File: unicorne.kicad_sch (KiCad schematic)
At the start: 17 parts, among them J1 Battery, J2 TPS43, J3 Expansion, J4 GPIO, J5 PAW3395 / PMW3360, Q1 AO3401A, Q2 2N7002, SW43 Power, SW44 Reset, U1 nice!nano v2

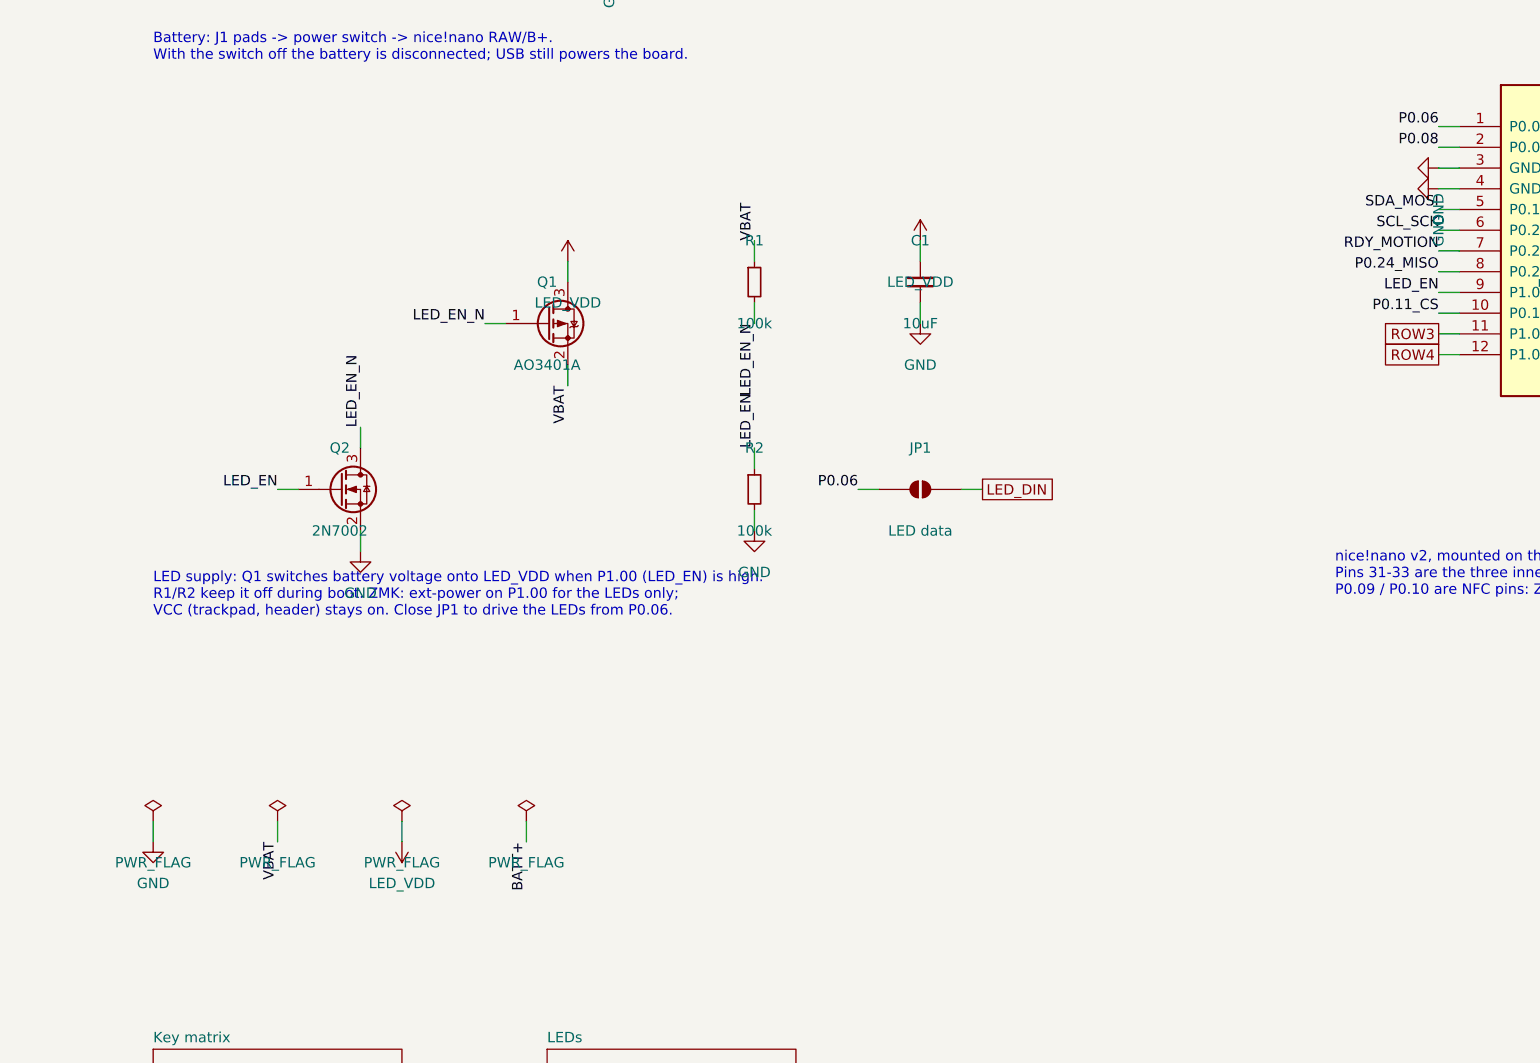
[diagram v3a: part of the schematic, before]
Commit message: Rework LED power, break lines and centre placement; add routing tools
- LED supply chosen by solder jumper JP2: nice!nano VCC, or an external
  supply on new LED IN pads (J6); never the battery pin. SN74LV1T125
  level shifter (U2) with bypass jumper JP3.
- Centre parts rearranged so the nice!nano's matrix pins are clear.
- 0805 hand-solder passives; LED chain runs left to right per row.
- Break lines: no sliver slots, perforated end to end, tabs over the lanes.
- Mounting holes stay inside the board and off the routing lanes.
- Routing tools (lanes, Freerouting driver, maze router) and placeholder
  STEP models. Boards are committed placed but unrouted.

Co-Authored-By: Claude Opus 5.5 <noreply@anthropic.com>
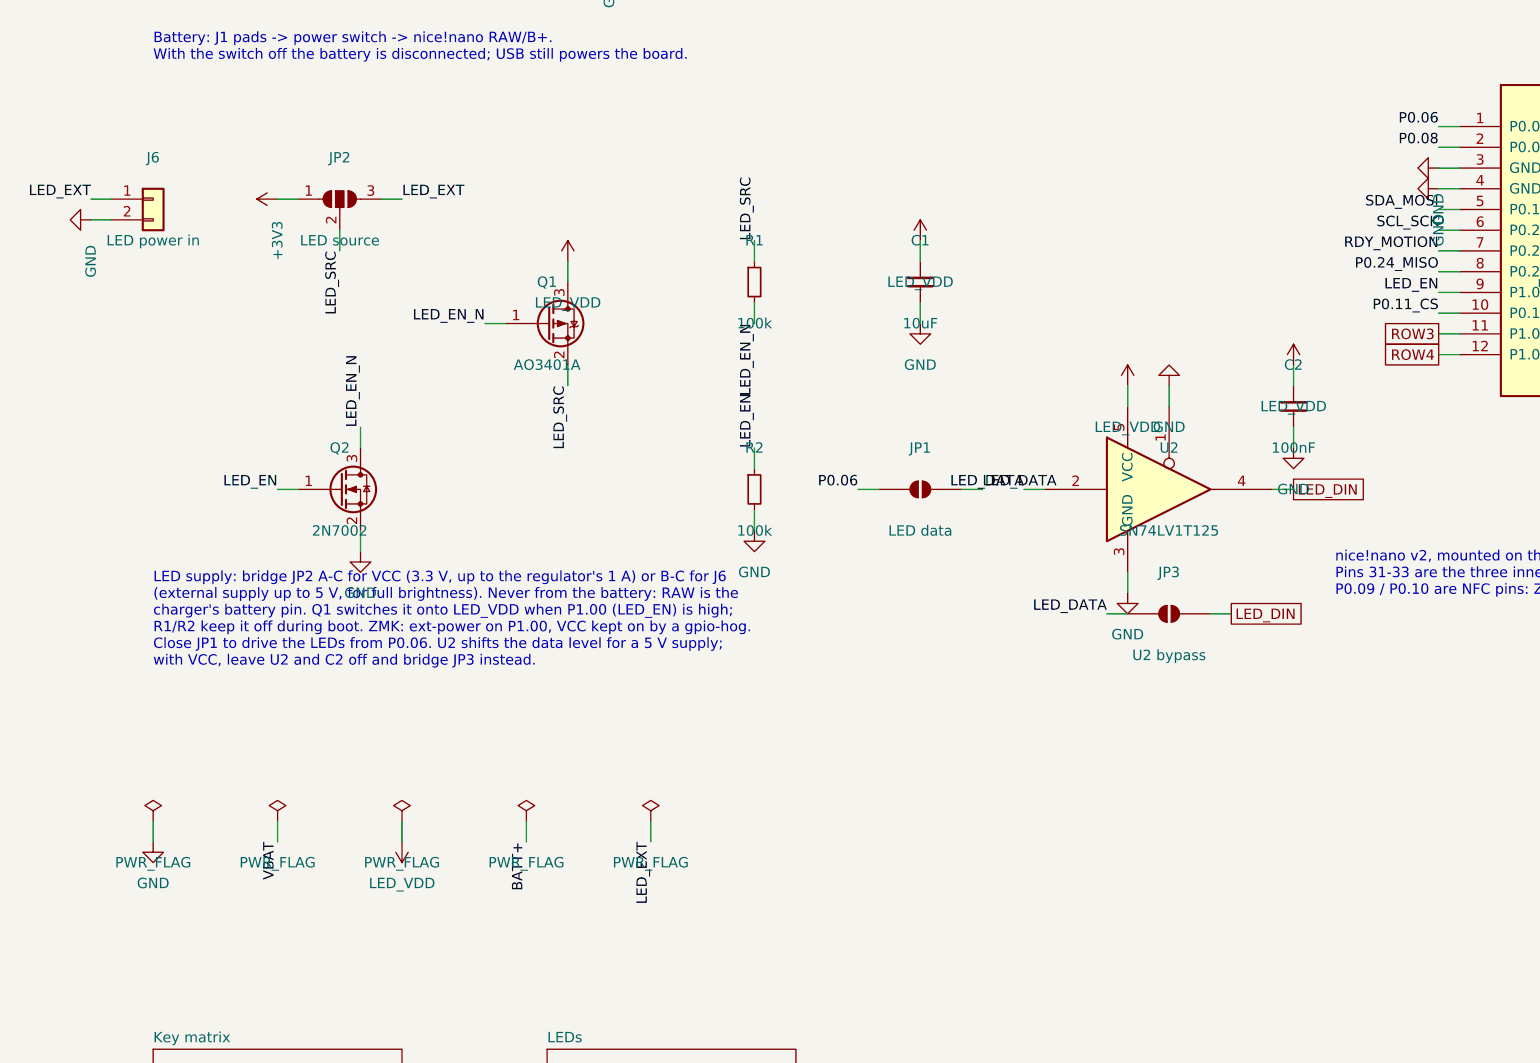
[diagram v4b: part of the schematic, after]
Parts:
- added C2: 100nF, Capacitor_SMD:C_0805_2012Metric_Pad1.18x1.45mm_HandSolder, symbol Device:C_Small
- added J6: LED power in, Connector_PinHeader_2.54mm:PinHeader_1x02_P2.54mm_Vertical, symbol Connector_Generic:Conn_01x02
- added JP2: LED source, Jumper:SolderJumper-3_P1.3mm_Open_RoundedPad1.0x1.5mm, symbol Jumper:SolderJumper_3_Open
- added JP3: U2 bypass, Jumper:SolderJumper-2_P1.3mm_Open_RoundedPad1.0x1.5mm, symbol Jumper:SolderJumper_2_Open
- added U2: SN74LV1T125, Package_TO_SOT_SMD:SOT-23-5_HandSoldering, symbol 74xGxx:74LVC1G125
- C1: footprint Capacitor_SMD:C_0805_2012Metric -> Capacitor_SMD:C_0805_2012Metric_Pad1.18x1.45mm_HandSolder
- R1, R2, R3, R4, R5: footprint Resistor_SMD:R_0603_1608Metric -> Resistor_SMD:R_0805_2012Metric_Pad1.20x1.40mm_HandSolder
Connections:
- net +3V3: now also JP2.1 (A)
- net GND: now also C2.2, J6.2 (Pin_2), U2.1, U2.3 (GND)
- net LED_DIN: now also JP3.2 (B), U2.4; no longer JP1.2 (B)
- net LED_VDD: now also C2.1, U2.5 (VCC)
- net VBAT: no longer Q1.2 (S), R1.1
- new net LED_DATA: JP1.2 (B), JP3.1 (A), U2.2
- new net LED_EXT: J6.1 (Pin_1), JP2.3 (B)
- new net LED_SRC: JP2.2 (C), Q1.2 (S), R1.1
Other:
- note added: "LED supply: bridge JP2 A-C for VCC (3.3 V, up to the regulator's 1 A) or B-C for J6 (external supply up to 5 V, for full brightness). Never from the battery: RAW is the charger's battery pin. Q1 switches it onto LED_VDD when P1.00 (LED_EN) is high; R1/R2 keep it off during boot. ZMK: ext-power on P1.00, VCC kept on by a gpio-hog. Close JP1 to drive the LEDs from P0.06. U2 shifts the data level fo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"
- note removed: "LED supply: Q1 switches battery voltage onto LED_VDD when P1.00 (LED_EN) is high. R1/R2 keep it off during boot. ZMK: ext-power on P1.00 for the LEDs only; VCC (trackpad, header) stays on. Close JP1 to drive the LEDs from P0.06."

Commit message: Add 3D models and STEP export
Project footprints point at models in lib/3d/: Kailh MX and Choc hotswap
sockets and the Choc V1 switch (keyswitch-kicad-library), plus placeholder
boxes for the nice!nano, TPS43, MX switch, SK6812MINI and MSK-12C02 (the
last two copied from the stock library with a model added). The trackpad
model sits on a board-only footprint; bare pads carry no model.
export_3d.py writes export/unicorne-{mx,choc}.step; renders alongside.

Both boards regenerated and re-routed: DRC 0 unconnected, 0 copper
violations.

Co-Authored-By: Claude Opus 5.5 <noreply@anthropic.com>
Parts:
- SW43: footprint Button_Switch_SMD:SW_SPDT_Shouhan_MSK12C02 -> unicorne:SW_SPDT_Shouhan_MSK12C02

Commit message: nice!nano and reset on top, TS-1136 H4.3 reset, USB notch; reroute both boards
- nice!nano moves to the top side, components up; the centre parts mirror so
  power switch and reset sit by RAW/RST and the LED parts and headers by
  P0.06. SMD parts stay on the bottom.
- Reset is now a TS-1136 H4.3 (6.0 x 3.5 mm, 2 pins 6.5 mm apart, 1.3 mm
  holes, from its drawing) on the top beside the nano.
- The board edge is notched for the nano's mid-mount USB-C, whose shell drops
  0.7 mm below the nano's underside.
- finish_route.py: 10 attempts by default, and dangling stubs are removed.
- Both boards rerouted: DRC 0 unconnected, schematic parity 0, every pin,
  the matrix and the LED chain verified. Gerbers, STEP, renders and plates
  regenerated.

Co-Authored-By: Claude Opus 5.5 <noreply@anthropic.com>
Claude-Session: https://claude.ai/code/session_01D39ubfTYtq6FMvNmmbStTo
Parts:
- SW44: footprint Button_Switch_THT:SW_PUSH_6mm_H5mm -> unicorne:SW_Tactile_SPST_3.5x6mm_H4.3mm_THT
